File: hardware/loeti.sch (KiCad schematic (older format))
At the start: 53 parts, among them J1 USB_C_Receptacle_USB2.0, J2 AudioJack3, J3 20021112-00014T1LF, Q1 BC817, Q2 BC817, Q3 BC807, Q4 Si4825DDY, DMG4435SSS, IRF939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, SW1 D6R, U1 AP2204R-3.3, U2 STUSB4500QTR, U3 STM32F030K6Tx, U4 TLV333-DBV, U5 INA239

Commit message: production version, v5
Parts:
- removed C10, C14, C5: 1μF 25V, Capacitor_SMD:C_0805_2012Metric_Pad1.18x1.45mm_HandSolder, symbol Device:C
- removed D3: BAT54S, Package_TO_SOT_SMD:SOT-23, symbol Diode:BAT54S
- removed R12: 20, Resistor_SMD:R_0603_1608Metric_Pad0.98x0.95mm_HandSolder, symbol Device:R
- removed U5: INA239, Package_SO:VSSOP-10_3x3mm_P0.5mm, symbol custom:INA239
- added D11: BZX84Cxx, Package_TO_SOT_SMD:TSOT-23_HandSoldering, symbol custom:BZX84Cxx
- added D3, D4, D8, D9: BAS16W, Package_TO_SOT_SMD:SOT-323_SC-70_Handsoldering, symbol Diode:BAS16W
- added R13, R7: 1k, Resistor_SMD:R_0603_1608Metric_Pad0.98x0.95mm_HandSolder, symbol Device:R
- added R14: 25k, Resistor_SMD:R_0603_1608Metric_Pad0.98x0.95mm_HandSolder, symbol Device:R
- added R16: 1M, Resistor_SMD:R_0603_1608Metric_Pad0.98x0.95mm_HandSolder, symbol Device:R
- added R17, R23, R24, R6: 10k, Resistor_SMD:R_0603_1608Metric_Pad0.98x0.95mm_HandSolder, symbol Device:R
- added R20: 20, Resistor_SMD:R_0603_1608Metric_Pad0.98x0.95mm_HandSolder, symbol Device:R
- added U4: 74AHC1G08, Package_TO_SOT_SMD:SOT-353_SC-70-5_Handsoldering, symbol 74xGxx:74AHC1G08
- added U5: INA301, Package_SO:VSSOP-8_3.0x3.0mm_P0.65mm, symbol custom:INA301
- added U6: TMP100, Package_TO_SOT_SMD:SOT-23-6_Handsoldering, symbol Sensor_Temperature:TMP100
- C10: renamed from C9; value 0.1μF -> 100n
- C11: value 1μF 25V -> 100n; footprint Capacitor_SMD:C_0805_2012Metric_Pad1.18x1.45mm_HandSolder -> Capacitor_SMD:C_0603_1608Metric_Pad1.08x0.95mm_HandSolder
- C12: renamed from C15; value 0.1μF -> 100n
- C13: renamed from C12; value 0.1μF -> 100n
- C14: renamed from C17; value 0.1μF -> 100n
- C3: renamed from C2; value 1μF 25V -> 1u
- C4: renamed from C3; value 1μF 25V -> 1u
- C5: renamed from C1; value 1μF 25V -> 4.7u
- C6: value 0.1μF -> 100n
- C7: renamed from C4; value 1μF 25V -> 4.7u
- C8: renamed from C7; value 0.1μF -> 100n
- C9: renamed from C8; value 0.1μF -> 100n
- D1: footprint Package_TO_SOT_SMD:SOT-323_SC-70 -> Package_TO_SOT_SMD:SOT-323_SC-70_Handsoldering
- D5: renamed from D4; footprint LED_THT:LED_D3.0mm -> LED_THT:LED_D1.8mm_W3.3mm_H2.4mm
- D6, D7: footprint LED_THT:LED_D3.0mm -> LED_THT:LED_D1.8mm_W3.3mm_H2.4mm
- J1: value USB_C_Receptacle_USB2.0 -> GCT USB4105; footprint Connector_USB:USB_C_Receptacle_GCT_USB4085 -> Connector_USB:USB_C_Receptacle_HRO_TYPE-C-31-M-12
- Q1, Q2, Q3: footprint Package_TO_SOT_SMD:SOT-23 -> Package_TO_SOT_SMD:SOT-23_Handsoldering
- R10: renamed from R14; value 1k -> 10k
- R11: renamed from R15; value 1k -> 10k
- R12: renamed from R16; value 1k -> 10k
- R18: renamed from R9; value 1k -> 10k
- U2: renamed from U1; footprint Package_TO_SOT_SMD:SOT-89-3 -> Package_TO_SOT_SMD:SOT-89-3_Handsoldering
- renumbered C13 to C1, C16 to C2, D5 to D10, R8 to R15, R13 to R19, R10 to R21, R11 to R22, R7 to R8, R6 to R9, U2 to U1, U4 to U7
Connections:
- net CURR_CS is gone; now on net SW: U3.2 (PF0)
- net SPI1_MISO is gone; now on net LED2: U3.27 (PB4)
- net SPI1_SCK is gone; now on net LED1: U3.26 (PB3)
- net +3V3: now also D11.3 (K), D3.3 (K), D8.3 (K), R16.1, R24.2, U4.5 (VCC), U5.1 (VS), U6.4 (V+)
- net ADC_IN2: now also R23.1; no longer C13.1, R21.1, U7.1
- net CURR_ALERT: now also U3.13 (PA7), R24.1, U4.2, U5.6 (nALERT); no longer U3.3 (PF1)
- net GND: now also D11.1 (A), D4.1 (A), D9.1 (A), R14.1, R7.1, U4.3 (GND), U5.4 (GND), U6.2 (GND), U6.3 (ADD1), U6.5 (ADD0)
- net I2C1_SCL: now also U6.1 (SCL)
- net I2C1_SDA: now also U6.6 (SDA)
- net LED0: now also U3.25 (PA15); no longer U3.9 (PA3)
- net LED1: no longer U3.10 (PA4)
- net LED2: no longer U3.11 (PA5)
- net PWM: now also U4.1; no longer R15.1
- net SW: no longer U3.25 (PA15)
- net T+: now also R16.2, R17.1; no longer U7.3 (+)
- net VBUS: now also C1.1, C2.1, Q2.3 (C), R18.2, R6.2, U5.8 (+); no longer C11.1
- net at Q4.4 (G): now also R20.2
- net at Q2.2 (E), Q3.2 (E): now also R20.1
- net CURR_RESET: now reaches U3.6 (PA0)
- net CURR_RESET: now also U5.5 (RESET)
- net ADC_IN1: now reaches U3.7 (PA1)
- net ADC_IN1: now also C11.1, R13.1
- net SPI1_MOSI: no longer names the net of U3.28 (PB5)
- net SPI1_NSS2: no longer names the net of U3.22 (PA12)
- net SWO: no longer names the net of J3.8 (JTDO/SWO)
- net VPP renamed SHUNT-
- net SHUNT-: now also U5.7 (-); no longer C1.1, C2.1, Q2.3 (C), R18.2
- new net: R15.1, U4.4
- new net: C13.1, R21.1, R23.2, U7.1
- new net: D8.1 (A), D9.3 (K), R17.2, U7.3 (+)
- new net: R13.2, U5.2 (OUT)
- new net: R14.2, U5.3 (LIMIT)
- new net ADC_IN3: D3.1 (A), D4.3 (K), R6.1, R7.2, U3.9 (PA3)
- no-connect marks 15 -> 23
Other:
- note added: "10 mOhm shunt\nGain 20 V/V\n0.2 V/A\n"
- note added: "1592 Hz low-pass"
- note added: "20 V Vgs, 20 V Vds \nminimum requirement for PMOS"
- note added: "Current limit:\n2.5 kOhm/A\n25 kOhm -> 10 A"
- note added: "Local temperature"
- note added: "Only C245\nSleeve: green (TC-, heater)\nRing: red (TC+)\nTip: blue (heater)"
- note added: "Thermocouple amplifier"
- note removed: "10 mOhm shunt"
- note removed: "20 V Vgs, 20 V Vds minimum requirement for PMOS"
- note removed: "ESD protection for ADC input"
- note removed: "Thermocouple ADC"
- moved on the sheet: C1, C12, C13, C14, C2, C3, C4, C5, C6, C7, D1, D10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

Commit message: firmware for v5
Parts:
- R13: value 1k -> 10k
- R18: value 10k -> 1k
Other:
- note added: "159.2 Hz low-pass"
- note removed: "1592 Hz low-pass"
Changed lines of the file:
@@
 P 12150 6300
 F 0 "R18" H 12219 6346 50  0000 L CNN
-F 1 "10k" H 12219 6255 50  0000 L CNN
+F 1 "1k" H 12219 6255 50  0000 L CNN
 F 2 "Resistor_SMD:R_0603_1608Metric_Pad0.98x0.95mm_HandSolder" V 12080 6300 50  0001 C CNN
 F 3 "~" H 12150 6300 50  0001 C CNN
@@
 P 11150 8800
 F 0 "R13" H 11219 8846 50  0000 L CNN
-F 1 "1k" H 11219 8755 50  0000 L CNN
+F 1 "10k" H 11219 8755 50  0000 L CNN
 F 2 "Resistor_SMD:R_0603_1608Metric_Pad0.98x0.95mm_HandSolder" V 11080 8800 50  0001 C CNN
 F 3 "~" H 11150 8800 50  0001 C CNN
@@
 	11300 8800 12200 8800
 Text Notes 10800 8500 0    50   ~ 0
-1592 Hz low-pass
+159.2 Hz low-pass
 Text Notes 11100 9850 0    50   ~ 0
 Current limit:\n2.5 kOhm/A\n25 kOhm -> 10 A

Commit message: software features fully working
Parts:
- C12, C13: value 100n -> DNP
- R10, R11, R12: value 10k -> 1k
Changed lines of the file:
@@
 P 14350 4650
 F 0 "C13" H 14465 4696 50  0000 L CNN
-F 1 "100n" H 14465 4605 50  0000 L CNN
+F 1 "DNP" H 14465 4605 50  0000 L CNN
 F 2 "Capacitor_SMD:C_0603_1608Metric_Pad1.08x0.95mm_HandSolder" H 14388 4500 50  0001 C CNN
 F 3 "~" H 14350 4650 50  0001 C CNN
@@
 P 11700 4550
 F 0 "C12" H 11815 4596 50  0000 L CNN
-F 1 "100n" H 11815 4505 50  0000 L CNN
+F 1 "DNP" H 11815 4505 50  0000 L CNN
 F 2 "Capacitor_SMD:C_0603_1608Metric_Pad1.08x0.95mm_HandSolder" H 11738 4400 50  0001 C CNN
 F 3 "~" H 11700 4550 50  0001 C CNN
@@
 P 8250 8700
 F 0 "R12" H 8319 8746 50  0000 L CNN
-F 1 "10k" H 8319 8655 50  0000 L CNN
+F 1 "1k" H 8319 8655 50  0000 L CNN
 F 2 "Resistor_SMD:R_0603_1608Metric_Pad0.98x0.95mm_HandSolder" V 8180 8700 50  0001 C CNN
 F 3 "~" H 8250 8700 50  0001 C CNN
@@
 P 7950 8450
 F 0 "R11" H 8019 8496 50  0000 L CNN
-F 1 "10k" H 8019 8405 50  0000 L CNN
+F 1 "1k" H 8019 8405 50  0000 L CNN
 F 2 "Resistor_SMD:R_0603_1608Metric_Pad0.98x0.95mm_HandSolder" V 7880 8450 50  0001 C CNN
 F 3 "~" H 7950 8450 50  0001 C CNN
@@
 P 7650 8200
 F 0 "R10" H 7719 8246 50  0000 L CNN
-F 1 "10k" H 7719 8155 50  0000 L CNN
+F 1 "1k" H 7719 8155 50  0000 L CNN
 F 2 "Resistor_SMD:R_0603_1608Metric_Pad0.98x0.95mm_HandSolder" V 7580 8200 50  0001 C CNN
 F 3 "~" H 7650 8200 50  0001 C CNN

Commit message: two-temperature mode
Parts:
- removed D7: LED, LED_THT:LED_D1.8mm_W3.3mm_H2.4mm, symbol Device:LED
- removed R12: 1k, Resistor_SMD:R_0603_1608Metric_Pad0.98x0.95mm_HandSolder, symbol Device:R
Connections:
- net GND: now also R10.1, R11.1; no longer D5.1 (K), D6.1 (K)
- net LED0: now also D5.2 (A); no longer R10.2
- net LED1: now also D6.2 (A); no longer R11.2
- new net: D5.1 (K), R10.2
- new net: D6.1 (K), R11.2
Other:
- moved on the sheet: D5, D6, R10, R11
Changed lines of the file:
@@
 LED0
-$Comp
-L Device:LED D5
-U 1 1 60A6F838
-P 8600 8200
-F 0 "D5" H 8593 8417 50  0000 C CNN
-F 1 "LED" H 8593 8326 50  0000 C CNN
-F 2 "LED_THT:LED_D1.8mm_W3.3mm_H2.4mm" H 8600 8200 50  0001 C CNN
-F 3 "~" H 8600 8200 50  0001 C CNN
-	1    8600 8200
-	-1   0    0    1
-$EndComp
-Wire Wire Line
-	8750 8200 9800 8200
-Wire Wire Line
-	9050 8450 9600 8450
-Wire Wire Line
-	9400 8700 9350 8700
-Wire Wire Line
-	9400 8800 9400 8700
 $Comp
 L power:GND #PWR036
@@
 	1    0    0    -1
 $EndComp
-$Comp
-L power:GND #PWR034
-U 1 1 60AE7307
-P 9400 8800
-F 0 "#PWR034" H 9400 8550 50  0001 C CNN
-F 1 "GND" H 9405 8627 50  0000 C CNN
-F 2 "" H 9400 8800 50  0001 C CNN
-F 3 "" H 9400 8800 50  0001 C CNN
-	1    9400 8800
-	1    0    0    -1
-$EndComp
-Wire Wire Line
-	8400 8700 9050 8700
-$Comp
-L Device:LED D7
-U 1 1 60A95747
-P 9200 8700
-F 0 "D7" H 9193 8917 50  0000 C CNN
-F 1 "LED" H 9193 8826 50  0000 C CNN
-F 2 "LED_THT:LED_D1.8mm_W3.3mm_H2.4mm" H 9200 8700 50  0001 C CNN
-F 3 "~" H 9200 8700 50  0001 C CNN
-	1    9200 8700
-	-1   0    0    1
-$EndComp
-$Comp
-L Device:LED D6
-U 1 1 60A952E3
-P 8900 8450
-F 0 "D6" H 8893 8667 50  0000 C CNN
-F 1 "LED" H 8893 8576 50  0000 C CNN
-F 2 "LED_THT:LED_D1.8mm_W3.3mm_H2.4mm" H 8900 8450 50  0001 C CNN
-F 3 "~" H 8900 8450 50  0001 C CNN
-	1    8900 8450
-	-1   0    0    1
-$EndComp
 Wire Wire Line
 	7500 9000 7450 9000
@@
 	1    0    0    -1
 $EndComp
-Wire Wire Line
-	8100 8450 8750 8450
-$Comp
-L Device:R R12
-U 1 1 60AC0274
-P 8250 8700
-F 0 "R12" H 8319 8746 50  0000 L CNN
-F 1 "1k" H 8319 8655 50  0000 L CNN
-F 2 "Resistor_SMD:R_0603_1608Metric_Pad0.98x0.95mm_HandSolder" V 8180 8700 50  0001 C CNN
-F 3 "~" H 8250 8700 50  0001 C CNN
-	1    8250 8700
-	0    1    1    0
-$EndComp
-$Comp
-L Device:R R11
-U 1 1 60ABFEAA
-P 7950 8450
-F 0 "R11" H 8019 8496 50  0000 L CNN
-F 1 "1k" H 8019 8405 50  0000 L CNN
-F 2 "Resistor_SMD:R_0603_1608Metric_Pad0.98x0.95mm_HandSolder" V 7880 8450 50  0001 C CNN
-F 3 "~" H 7950 8450 50  0001 C CNN
-	1    7950 8450
-	0    1    1    0
-$EndComp
-Wire Wire Line
-	7450 8700 8100 8700
-Wire Wire Line
-	7450 8450 7800 8450
-Text GLabel 7450 8700 0    50   Input ~ 0
-LED2
 Text GLabel 7450 8450 0    50   Input ~ 0
 LED1
-Wire Wire Line
-	8450 8200 7800 8200
-$Comp
-L Device:R R10
-U 1 1 60ABF026
-P 7650 8200
-F 0 "R10" H 7719 8246 50  0000 L CNN
-F 1 "1k" H 7719 8155 50  0000 L CNN
-F 2 "Resistor_SMD:R_0603_1608Metric_Pad0.98x0.95mm_HandSolder" V 7580 8200 50  0001 C CNN
-F 3 "~" H 7650 8200 50  0001 C CNN
-	1    7650 8200
-	0    1    1    0
-$EndComp
 Wire Wire Line
 	7450 8200 7500 8200
@@
 Text Notes 5250 8550 0    50   ~ 0
 Only C245\nSleeve: green (TC-, heater)\nRing: red (TC+)\nTip: blue (heater)
+$Comp
+L Device:LED D5
+U 1 1 60A6F838
+P 7650 8200
+F 0 "D5" H 7643 8417 50  0000 C CNN
+F 1 "LED" H 7643 8326 50  0000 C CNN
+F 2 "LED_THT:LED_D1.8mm_W3.3mm_H2.4mm" H 7650 8200 50  0001 C CNN
+F 3 "~" H 7650 8200 50  0001 C CNN
+	1    7650 8200
+	-1   0    0    1
+$EndComp
+Wire Wire Line
+	7800 8200 8850 8200
+Wire Wire Line
+	8100 8450 8650 8450
+$Comp
+L Device:LED D6
+U 1 1 60A952E3
+P 7950 8450
+F 0 "D6" H 7943 8667 50  0000 C CNN
+F 1 "LED" H 7943 8576 50  0000 C CNN
+F 2 "LED_THT:LED_D1.8mm_W3.3mm_H2.4mm" H 7950 8450 50  0001 C CNN
+F 3 "~" H 7950 8450 50  0001 C CNN
+	1    7950 8450
+	-1   0    0    1
+$EndComp
+Wire Wire Line
+	7800 8450 7450 8450
+Wire Wire Line
+	9800 8200 9150 8200
+$Comp
+L Device:R R10
+U 1 1 60ABF026
+P 9000 8200
+F 0 "R10" H 9069 8246 50  0000 L CNN
+F 1 "1k" H 9069 8155 50  0000 L CNN
+F 2 "Resistor_SMD:R_0603_1608Metric_Pad0.98x0.95mm_HandSolder" V 8930 8200 50  0001 C CNN
+F 3 "~" H 9000 8200 50  0001 C CNN
+	1    9000 8200
+	0    1    1    0
+$EndComp
+$Comp
+L Device:R R11
+U 1 1 60ABFEAA
+P 8800 8450
+F 0 "R11" H 8869 8496 50  0000 L CNN
+F 1 "1k" H 8869 8405 50  0000 L CNN
+F 2 "Resistor_SMD:R_0603_1608Metric_Pad0.98x0.95mm_HandSolder" V 8730 8450 50  0001 C CNN
+F 3 "~" H 8800 8450 50  0001 C CNN
+	1    8800 8450
+	0    1    1    0
+$EndComp
+Wire Wire Line
+	8950 8450 9600 8450
 $EndSCHEMATC

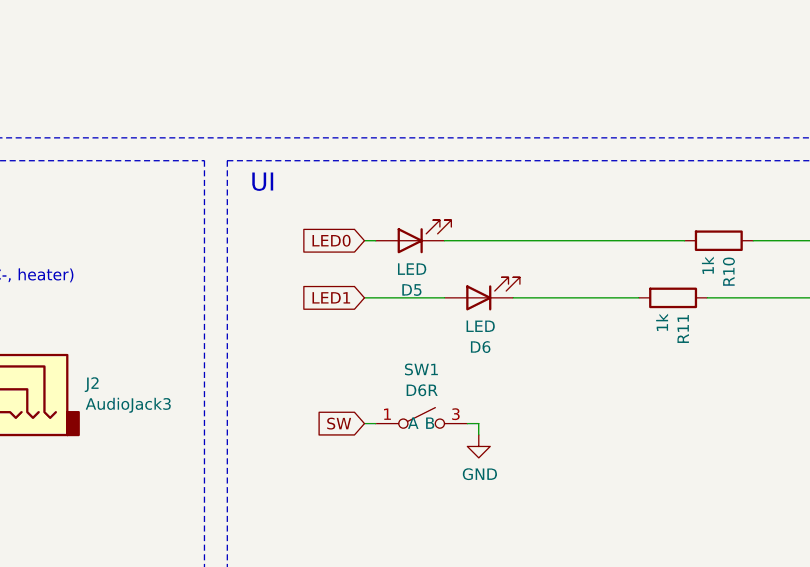
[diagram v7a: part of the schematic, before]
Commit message: improved display v5b complete
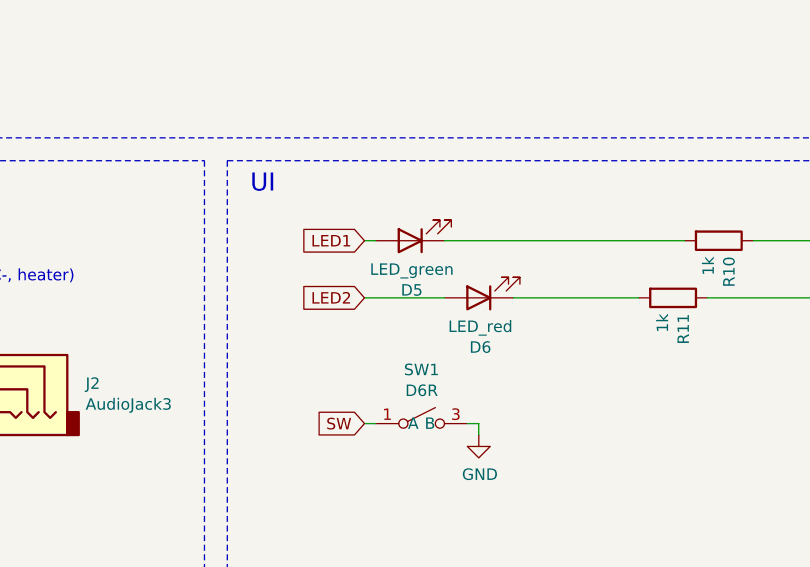
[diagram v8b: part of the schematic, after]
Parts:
- D5: value LED -> LED_green
- D6: value LED -> LED_red
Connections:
- net LED0: no longer D5.2 (A)
- net LED1: now also D5.2 (A); no longer D6.2 (A)
- net LED2: now also D6.2 (A)
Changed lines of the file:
@@
 $EndComp
 Text GLabel 7450 8450 0    50   Input ~ 0
-LED1
+LED2
 Wire Wire Line
 	7450 8200 7500 8200
 Text GLabel 7450 8200 0    50   Input ~ 0
-LED0
+LED1
 Wire Wire Line
 	13200 3950 13200 4000
@@
 P 7650 8200
 F 0 "D5" H 7643 8417 50  0000 C CNN
-F 1 "LED" H 7643 8326 50  0000 C CNN
+F 1 "LED_green" H 7643 8326 50  0000 C CNN
 F 2 "LED_THT:LED_D1.8mm_W3.3mm_H2.4mm" H 7650 8200 50  0001 C CNN
 F 3 "~" H 7650 8200 50  0001 C CNN
@@
 P 7950 8450
 F 0 "D6" H 7943 8667 50  0000 C CNN
-F 1 "LED" H 7943 8576 50  0000 C CNN
+F 1 "LED_red" H 7943 8576 50  0000 C CNN
 F 2 "LED_THT:LED_D1.8mm_W3.3mm_H2.4mm" H 7950 8450 50  0001 C CNN
 F 3 "~" H 7950 8450 50  0001 C CNN
